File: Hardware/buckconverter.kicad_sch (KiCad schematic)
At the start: 16 parts, among them U7 TPS54332DDA

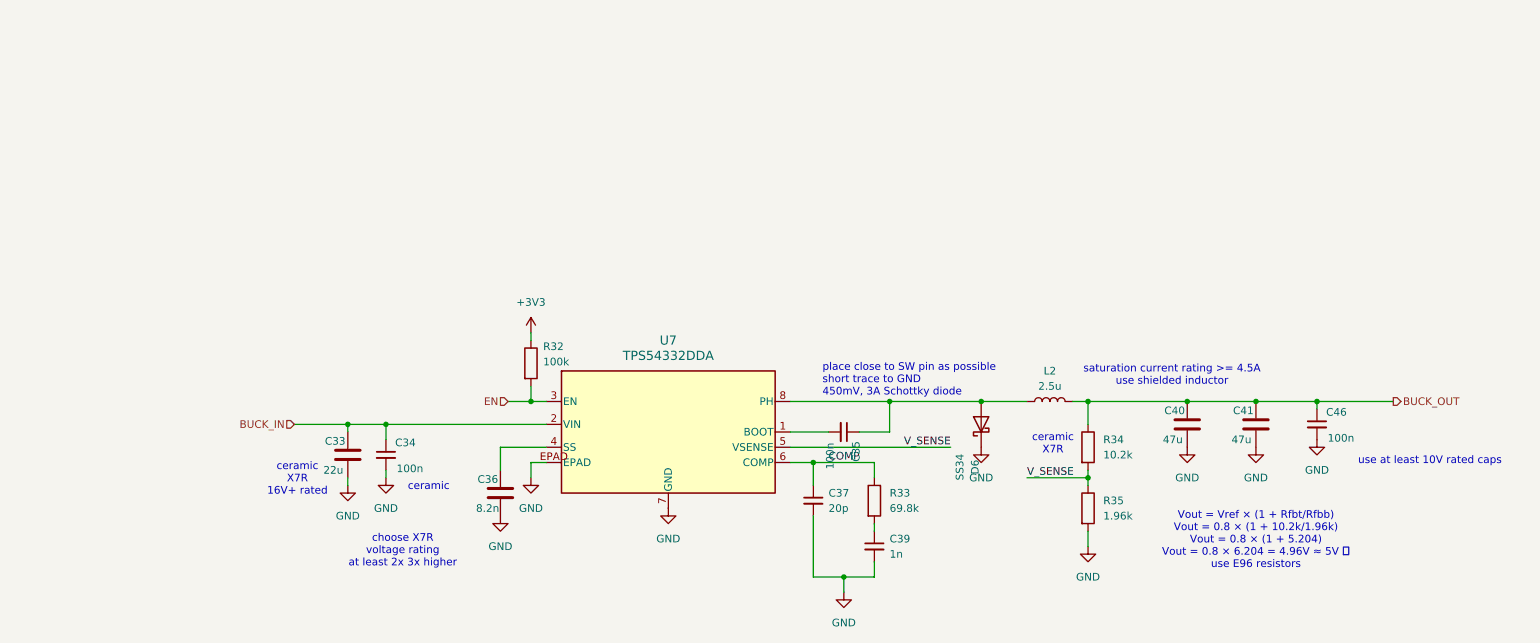
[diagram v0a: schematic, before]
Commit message: reorganization into 4 sheets, schematic not finalized yet
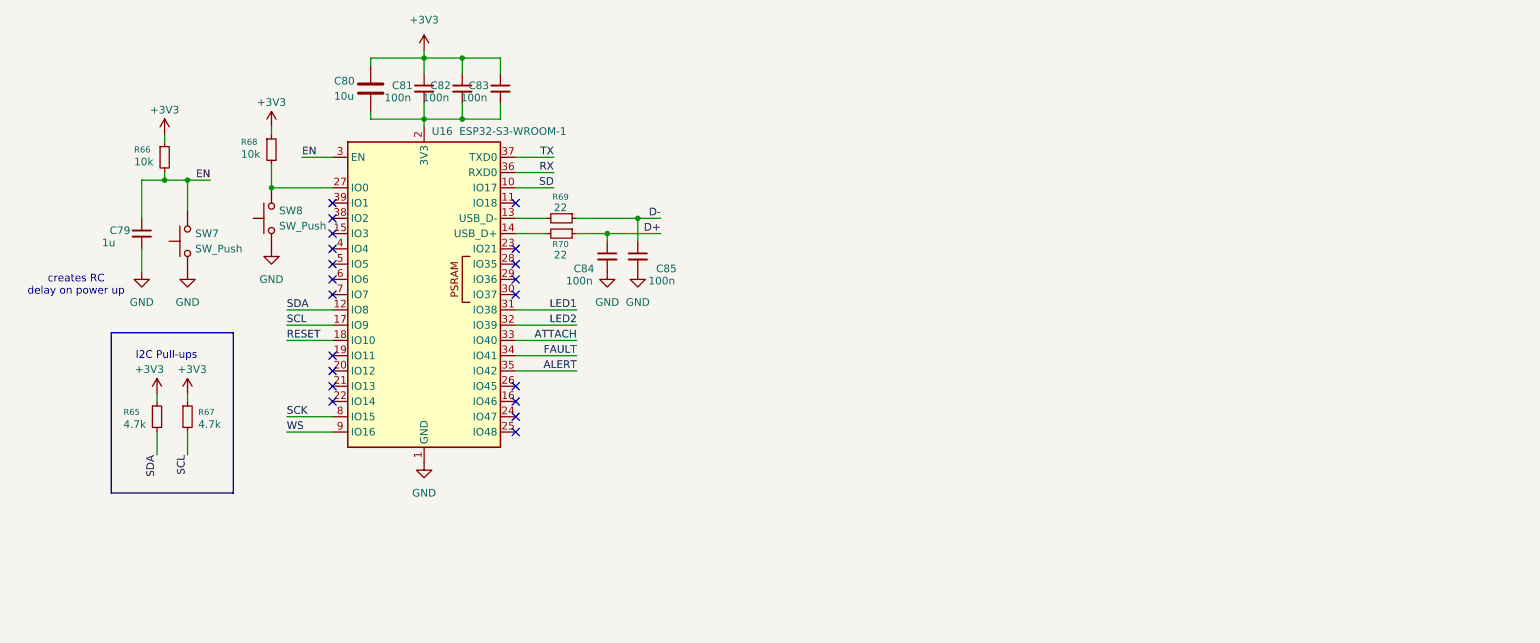
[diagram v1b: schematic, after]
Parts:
- removed C33: 22u, symbol Device:C
- removed C34, C35, C46: 100n, symbol Device:C_Small
- removed C36: 8.2n, symbol Device:C
- removed C37: 20p, symbol Device:C_Small
- removed C39: 1n, symbol Device:C_Small
- removed C40, C41: 47u, symbol Device:C
- removed D6: SS34, Diode_SMD:D_SMA, symbol Diode:SS34
- removed L2: 2.5u, symbol Device:L
- removed R32: 100k, symbol Device:R
- removed R33: 69.8k, symbol Device:R
- removed R34: 10.2k, symbol Device:R
- removed R35: 1.96k, symbol Device:R
- removed U7: TPS54332DDA, DDA8_3X2P13, symbol LED Sign:TPS54332DDA
- added C79: 1u, symbol Device:C_Small
- added C80: 10u, symbol Device:C
- added C81, C82, C83, C84, C85: 100n, symbol Device:C_Small
- added R65, R67: 4.7k, symbol Device:R_Small
- added R66, R68: 10k, symbol Device:R_Small
- added R69, R70: 22, symbol Device:R_Small
- added SW7, SW8: SW_Push, symbol Switch:SW_Push
- added U16: ESP32-S3-WROOM-1, RF_Module:ESP32-S3-WROOM-1, symbol RF_Module:ESP32-S3-WROOM-1
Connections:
- net +3V3: now also C80.2, C81.1, C82.1, C83.1, R65.1, R66.1, R67.1, R68.1
- net EN: now also C79.1, R66.2, SW7.2, U16.3 (EN)
- net GND: now also C79.2, C84.2, C85.2, SW7.1, SW8.1, U16.1 (GND), U16.40 (GND), U16.41 (GND)
- new net: C80.1, C81.2, C82.2, C83.2, U16.2 (3V3)
- new net: R69.2, U16.13 (USB_D-)
- new net: R70.2, U16.14 (USB_D+)
- new net: R68.2, SW8.2, U16.27 (IO0)
- new net ALERT: U16.35 (IO42)
- new net ATTACH: U16.33 (IO40)
- new net D+: C84.1, R70.1
- new net D-: C85.1, R69.1
- new net FAULT: U16.34 (IO41)
- new net LED1: U16.31 (IO38)
- new net LED2: U16.32 (IO39)
- new net RESET: U16.18 (IO10)
- new net RX: U16.36 (RXD0)
- new net SCK: U16.8 (IO15)
- new net SCL: R67.2, U16.17 (IO9)
- new net SD: U16.10 (IO17)
- new net SDA: R65.2, U16.12 (IO8)
- new net TX: U16.37 (TXD0)
- new net WS: U16.9 (IO16)
- no-connect marks 0 -> 20
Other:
- note added: "I2C Pull-ups"
- note added: "creates RC delay on power up"
- note removed: "Vout = Vref × (1 + Rfbt/Rfbb) Vout = 0.8 × (1 + 10.2k/1.96k) Vout = 0.8 × (1 + 5.204) Vout = 0.8 × 6.204 = 4.96V ≈ 5V ✅ use E96 resistors"
- note removed: "ceramic"
- note removed: "ceramic X7R"
- note removed: "ceramic X7R 16V+ rated"
- note removed: "choose X7R voltage rating at least 2x 3x higher"
- note removed: "place close to SW pin as possible short trace to GND 450mV, 3A Schottky diode"
- note removed: "saturation current rating >= 4.5A use shielded inductor"
- note removed: "use at least 10V rated caps"
